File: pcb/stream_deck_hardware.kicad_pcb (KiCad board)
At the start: 2 copper layers, 16 parts, among them SW1 SW_Push_LED, SW10 SW_Push_LED, SW11 SW_Push_LED, SW3 SW_Push_LED, SW5 SW_Push_LED, SW6 SW_Push_LED, SW8 SW_Push_LED, SW9 SW_Push_LED

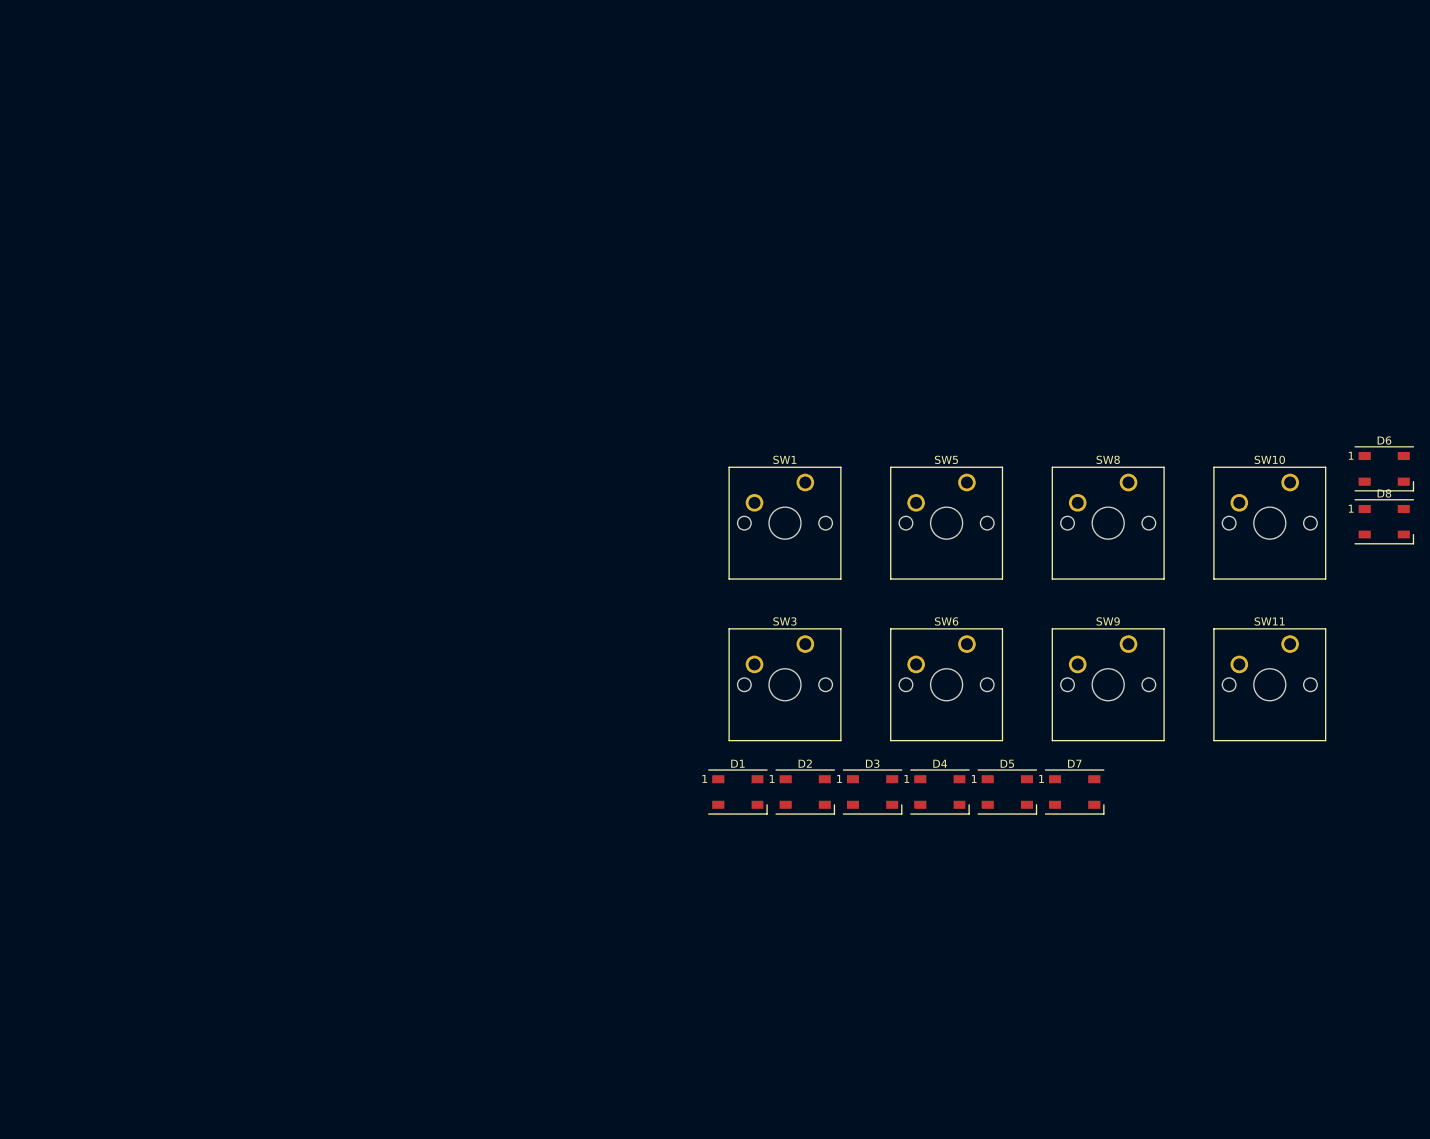
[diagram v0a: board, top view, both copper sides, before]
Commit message: Footprints update and some changes
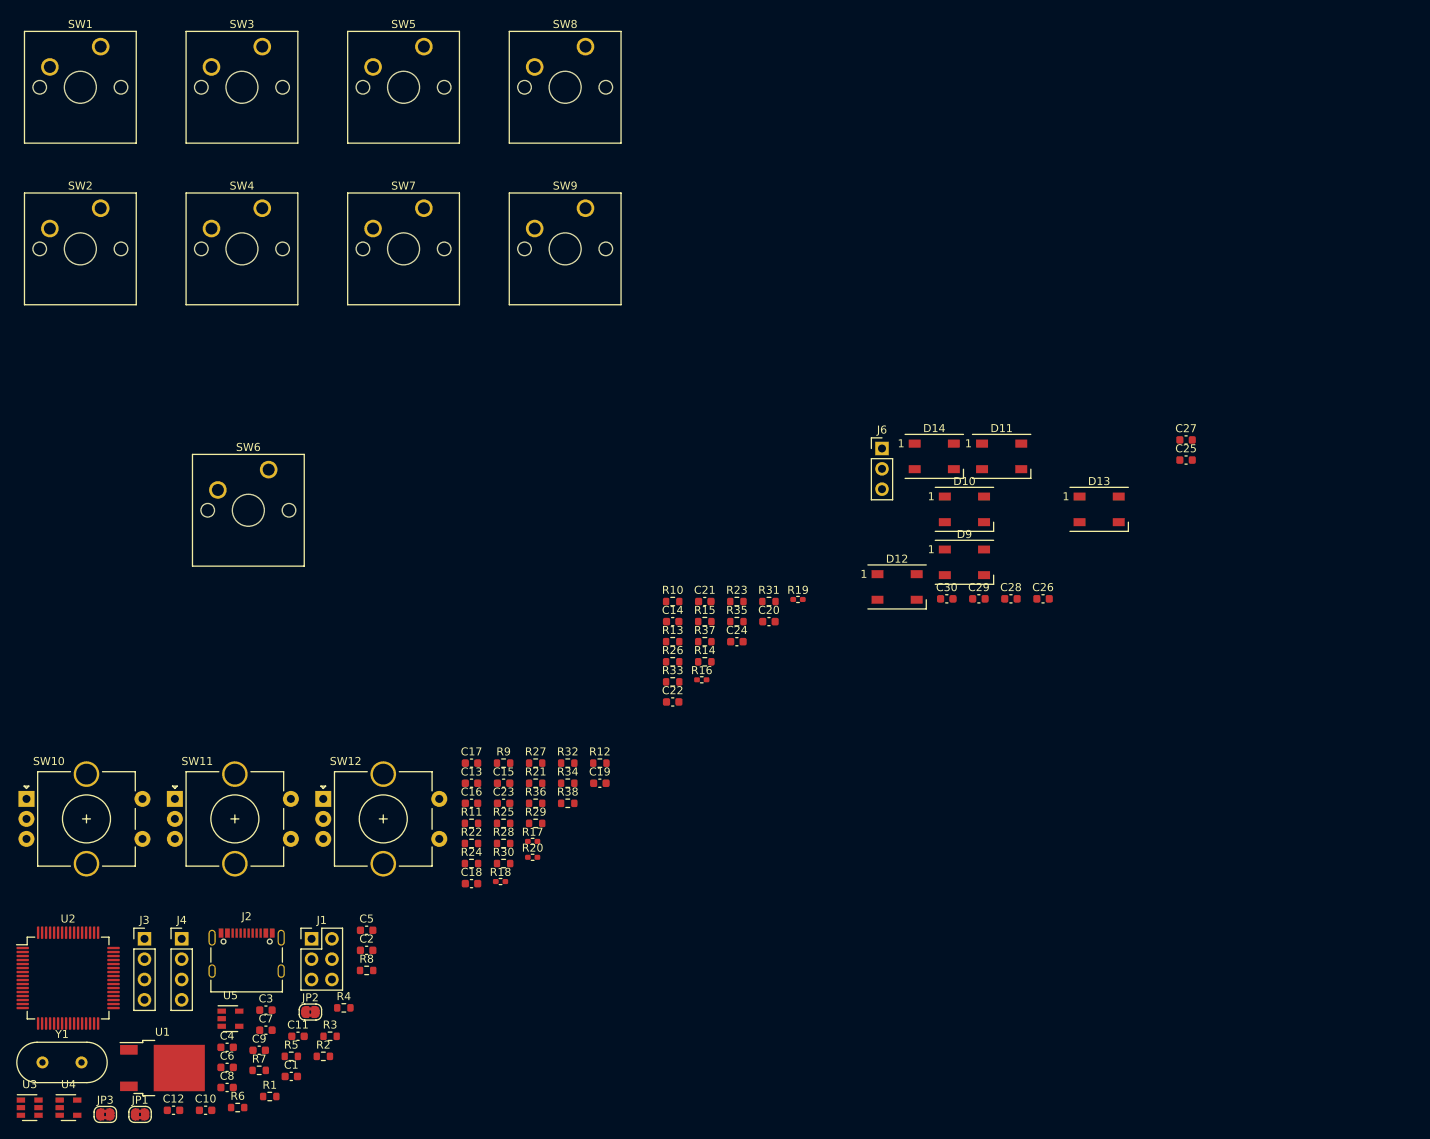
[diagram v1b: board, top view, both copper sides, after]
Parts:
- removed D1, D2, D3, D4, D5, D6, D7, D8: WS2812B, LED_SMD:LED_WS2812B_PLCC4_5.0x5.0mm_P3.2mm
- added C1: 100nF, Capacitor_SMD:C_0603_1608Metric, F.Cu at (56.2, 97.5)
- added C10: 25pF, Capacitor_SMD:C_0603_1608Metric, F.Cu at (45.5, 101.8)
- added C11: 25pF, Capacitor_SMD:C_0603_1608Metric, F.Cu at (57.0, 92.5)
- added C12: 0.1uF, Capacitor_SMD:C_0603_1608Metric, F.Cu at (41.5, 101.8)
- added C13: C, Capacitor_SMD:C_0603_1608Metric, F.Cu at (78.7, 60.9)
- added C14: C, Capacitor_SMD:C_0603_1608Metric, F.Cu at (103.9, 40.7)
- added C15: C, Capacitor_SMD:C_0603_1608Metric, F.Cu at (82.7, 60.9)
- added C16: C, Capacitor_SMD:C_0603_1608Metric, F.Cu at (78.7, 63.4)
- added C17: C, Capacitor_SMD:C_0603_1608Metric, F.Cu at (78.7, 58.4)
- added C18: C, Capacitor_SMD:C_0603_1608Metric, F.Cu at (78.7, 73.5)
- added C19: C, Capacitor_SMD:C_0603_1608Metric, F.Cu at (94.7, 60.9)
- added C2: 100nF, Capacitor_SMD:C_0603_1608Metric, F.Cu at (65.6, 81.8)
- added C20: C, Capacitor_SMD:C_0603_1608Metric, F.Cu at (115.9, 40.7)
- added C21: C, Capacitor_SMD:C_0603_1608Metric, F.Cu at (107.9, 38.2)
- added C22: C, Capacitor_SMD:C_0603_1608Metric, F.Cu at (103.9, 50.7)
- added C23: C, Capacitor_SMD:C_0603_1608Metric, F.Cu at (82.7, 63.4)
- added C24: C, Capacitor_SMD:C_0603_1608Metric, F.Cu at (111.9, 43.2)
- added C25: C, Capacitor_SMD:C_0603_1608Metric, F.Cu at (168.0, 20.5)
- added C26: C, Capacitor_SMD:C_0603_1608Metric, F.Cu at (150.1, 37.9)
- added C27: C, Capacitor_SMD:C_0603_1608Metric, F.Cu at (168.0, 18.0)
- added C28: C, Capacitor_SMD:C_0603_1608Metric, F.Cu at (146.1, 37.9)
- added C29: C, Capacitor_SMD:C_0603_1608Metric, F.Cu at (142.1, 37.9)
- added C3: 100nF, Capacitor_SMD:C_0603_1608Metric, F.Cu at (53.0, 89.3)
- added C30: C, Capacitor_SMD:C_0603_1608Metric, F.Cu at (138.1, 37.9)
- added C4: 100nF, Capacitor_SMD:C_0603_1608Metric, F.Cu at (48.2, 93.9)
- added C5: 100nF, Capacitor_SMD:C_0603_1608Metric, F.Cu at (65.6, 79.3)
- added C6: 100nF, Capacitor_SMD:C_0603_1608Metric, F.Cu at (48.2, 96.4)
- added C7: 0,1uF, Capacitor_SMD:C_0603_1608Metric, F.Cu at (53.0, 91.8)
- added C8: 2,2uF, Capacitor_SMD:C_0603_1608Metric, F.Cu at (48.2, 98.9)
- added C9: 4.7uF, Capacitor_SMD:C_0603_1608Metric, F.Cu at (52.2, 94.3)
- added D10: WS2812B, LED_SMD:LED_WS2812B_PLCC4_5.0x5.0mm_P3.2mm, F.Cu at (140.3, 26.7)
- added D11: WS2812B, LED_SMD:LED_WS2812B_PLCC4_5.0x5.0mm_P3.2mm, F.Cu at (145.0, 20.0)
- added D12: WS2812B, LED_SMD:LED_WS2812B_PLCC4_5.0x5.0mm_P3.2mm, F.Cu at (131.9, 36.4)
- added D13: WS2812B, LED_SMD:LED_WS2812B_PLCC4_5.0x5.0mm_P3.2mm, F.Cu at (157.2, 26.7)
- added D14: WS2812B, LED_SMD:LED_WS2812B_PLCC4_5.0x5.0mm_P3.2mm, F.Cu at (136.6, 20.0)
- added D9: WS2812B, LED_SMD:LED_WS2812B_PLCC4_5.0x5.0mm_P3.2mm, F.Cu at (140.3, 33.3)
- added J1: Conn_BOOT, Connector_PinHeader_2.54mm:PinHeader_2x03_P2.54mm_Vertical, F.Cu at (58.7, 80.3)
- added J2: USB_C_Receptacle_USB2.0, Connector_USB:USB_C_Receptacle_Palconn_UTC16-G, F.Cu at (50.6, 82.1)
- added J3: Conn_01x04_Male, Connector_PinHeader_2.54mm:PinHeader_1x04_P2.54mm_Vertical, F.Cu at (37.8, 80.3)
- added J4: Conn_01x04_Male, Connector_PinHeader_2.54mm:PinHeader_1x04_P2.54mm_Vertical, F.Cu at (42.5, 80.3)
- added J6: Conn_01x03_Female, Connector_PinHeader_2.54mm:PinHeader_1x03_P2.54mm_Vertical, F.Cu at (130.0, 19.1)
- added JP1: SolderJumper_2_Bridged, Jumper:SolderJumper-2_P1.3mm_Bridged2Bar_RoundedPad1.0x1.5mm, F.Cu at (37.3, 102.3)
- added JP2: SolderJumper_2_Bridged, Jumper:SolderJumper-2_P1.3mm_Bridged2Bar_RoundedPad1.0x1.5mm, F.Cu at (58.6, 89.5)
- added JP3: SolderJumper_2_Bridged, Jumper:SolderJumper-2_P1.3mm_Bridged2Bar_RoundedPad1.0x1.5mm, F.Cu at (32.9, 102.3)
- added R1: R, Resistor_SMD:R_0603_1608Metric, F.Cu at (53.5, 100.1)
- added R10: R, Resistor_SMD:R_0603_1608Metric, F.Cu at (103.9, 38.2)
- added R11: R, Resistor_SMD:R_0603_1608Metric, F.Cu at (78.7, 65.9)
- added R12: R, Resistor_SMD:R_0603_1608Metric, F.Cu at (94.7, 58.4)
- added R13: R, Resistor_SMD:R_0603_1608Metric, F.Cu at (103.9, 43.2)
- added R14: R, Resistor_SMD:R_0603_1608Metric, F.Cu at (107.9, 45.7)
- added R15: R, Resistor_SMD:R_0603_1608Metric, F.Cu at (107.9, 40.7)
- added R16: R, Resistor_SMD:R_0402_1005Metric_Pad0.72x0.64mm_HandSolder, F.Cu at (107.5, 48.0)
- added R17: R, Resistor_SMD:R_0402_1005Metric_Pad0.72x0.64mm_HandSolder, F.Cu at (86.3, 68.2)
- added R18: R, Resistor_SMD:R_0402_1005Metric_Pad0.72x0.64mm_HandSolder, F.Cu at (82.3, 73.2)
- added R19: R, Resistor_SMD:R_0402_1005Metric_Pad0.72x0.64mm_HandSolder, F.Cu at (119.5, 37.9)
- added R2: R, Resistor_SMD:R_0603_1608Metric, F.Cu at (60.2, 95.0)
- added R20: R, Resistor_SMD:R_0402_1005Metric_Pad0.72x0.64mm_HandSolder, F.Cu at (86.3, 70.2)
- added R21: R, Resistor_SMD:R_0603_1608Metric, F.Cu at (86.7, 60.9)
- added R22: R, Resistor_SMD:R_0603_1608Metric, F.Cu at (78.7, 68.4)
- added R23: R, Resistor_SMD:R_0603_1608Metric, F.Cu at (111.9, 38.2)
- added R24: R, Resistor_SMD:R_0603_1608Metric, F.Cu at (78.7, 70.9)
- added R25: R, Resistor_SMD:R_0603_1608Metric, F.Cu at (82.7, 65.9)
- added R26: R, Resistor_SMD:R_0603_1608Metric, F.Cu at (103.9, 45.7)
- added R27: R, Resistor_SMD:R_0603_1608Metric, F.Cu at (86.7, 58.4)
- added R28: R, Resistor_SMD:R_0603_1608Metric, F.Cu at (82.7, 68.4)
- added R29: R, Resistor_SMD:R_0603_1608Metric, F.Cu at (86.7, 65.9)
- added R3: 5.1k, Resistor_SMD:R_0603_1608Metric, F.Cu at (61.0, 92.5)
- added R30: R, Resistor_SMD:R_0603_1608Metric, F.Cu at (82.7, 70.9)
- added R31: R, Resistor_SMD:R_0603_1608Metric, F.Cu at (115.9, 38.2)
- added R32: R, Resistor_SMD:R_0603_1608Metric, F.Cu at (90.7, 58.4)
- added R33: R, Resistor_SMD:R_0603_1608Metric, F.Cu at (103.9, 48.2)
- added R34: R, Resistor_SMD:R_0603_1608Metric, F.Cu at (90.7, 60.9)
- added R35: R, Resistor_SMD:R_0603_1608Metric, F.Cu at (111.9, 40.7)
- added R36: R, Resistor_SMD:R_0603_1608Metric, F.Cu at (86.7, 63.4)
- added R37: R, Resistor_SMD:R_0603_1608Metric, F.Cu at (107.9, 43.2)
- added R38: R, Resistor_SMD:R_0603_1608Metric, F.Cu at (90.7, 63.4)
- added R4: 5.1k, Resistor_SMD:R_0603_1608Metric, F.Cu at (62.7, 89.0)
- added R5: R, Resistor_SMD:R_0603_1608Metric, F.Cu at (56.2, 95.0)
- added R6: 4k7, Resistor_SMD:R_0603_1608Metric, F.Cu at (49.5, 101.4)
- added R7: 4k7, Resistor_SMD:R_0603_1608Metric, F.Cu at (52.2, 96.8)
- added R8: 4k7, Resistor_SMD:R_0603_1608Metric, F.Cu at (65.6, 84.3)
- added R9: R, Resistor_SMD:R_0603_1608Metric, F.Cu at (82.7, 58.4)
- added SW12: EN_03, Rotary_Encoder:RotaryEncoder_Alps_EC11E-Switch_Vertical_H20mm_CircularMountingHoles, F.Cu at (60.2, 62.9)
- added SW2: SW_Push, Button_Switch_Keyboard:SW_Cherry_MX_1.00u_PCB, F.Cu at (32.4, -11.0)
- added SW4: SW_Push, Button_Switch_Keyboard:SW_Cherry_MX_1.00u_PCB, F.Cu at (52.5, -11.0)
- added SW7: SW_Push, Button_Switch_Keyboard:SW_Cherry_MX_1.00u_PCB, F.Cu at (72.8, -11.0)
- added U1: LF33_TO252, Package_TO_SOT_SMD:TO-252-2, F.Cu at (40.1, 96.5)
- added U2: STM32F401RCTx, Package_QFP:LQFP-64_10x10mm_P0.5mm, F.Cu at (28.3, 85.2)
- added U3: 74LVC1G332, Package_TO_SOT_SMD:SOT-23-6, F.Cu at (23.5, 101.5)
- added U4: AT24CS02-STUM, Package_TO_SOT_SMD:SOT-23-5, F.Cu at (28.3, 101.5)
- added U5: AT24CS02-STUM, Package_TO_SOT_SMD:SOT-23-5, F.Cu at (48.6, 90.3)
- added Y1: Crystal_Small, Crystal:Crystal_HC49-U_Vertical, F.Cu at (25.1, 95.8)
- SW1, SW3, SW5, SW6, SW8, SW9: value SW_Push_LED -> SW_Push
- SW10: value SW_Push_LED -> EN_01; footprint Button_Switch_Keyboard:SW_Cherry_MX_1.00u_PCB -> Rotary_Encoder:RotaryEncoder_Alps_EC11E-Switch_Vertical_H20mm_CircularMountingHoles
- SW11: value SW_Push_LED -> EN_02; footprint Button_Switch_Keyboard:SW_Cherry_MX_1.00u_PCB -> Rotary_Encoder:RotaryEncoder_Alps_EC11E-Switch_Vertical_H20mm_CircularMountingHoles
- moved SW10 162.8 mm to (23.1, 62.9)
- moved SW11 140.7 mm to (41.6, 62.9)
- moved SW1 103.6 mm to (32.4, -31.2)
- moved SW3 100.9 mm to (52.5, -31.2)
- moved SW6 90.0 mm to (53.4, 21.7)
- moved SW8 87.0 mm to (93.0, -31.2)
- moved SW9 87.0 mm to (93.0, -11.0)
- moved SW5 87.0 mm to (72.8, -31.2)
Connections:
- SW1 pad 1: (no net) -> Net-(C13-Pad1)
- SW1 pad 2: (no net) -> GND
- SW3 pad 1: (no net) -> Net-(C15-Pad1)
- SW3 pad 2: (no net) -> GND
- SW5 pad 1: (no net) -> Net-(C17-Pad1)
- SW5 pad 2: (no net) -> GND
- SW6 pad 1: (no net) -> Net-(C18-Pad1)
- SW6 pad 2: (no net) -> GND
- SW8 pad 1: (no net) -> Net-(C20-Pad1)
- SW8 pad 2: (no net) -> GND
- SW9 pad 1: (no net) -> Net-(C21-Pad1)
- SW9 pad 2: (no net) -> GND

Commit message: PCB edges prototype
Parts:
- moved R3 200.0 mm to (254.5, 143.3)
- moved R4 198.4 mm to (254.7, 138.9)
- moved C5 196.2 mm to (254.8, 131.2)
- moved C2 196.2 mm to (254.8, 133.7)
- moved R8 196.2 mm to (254.8, 136.2)
- moved C14 165.4 mm to (254.0, 110.1)
- moved C20 165.4 mm to (266.1, 110.1)
- moved C21 165.4 mm to (258.0, 107.6)
- moved C22 165.4 mm to (254.0, 120.1)
- moved C24 165.4 mm to (262.1, 112.6)
- moved R10 165.4 mm to (254.0, 107.6)
- moved R13 165.4 mm to (254.0, 112.6)
- moved R14 165.4 mm to (258.0, 115.1)
- moved R15 165.4 mm to (258.0, 110.1)
- moved R16 165.4 mm to (257.7, 117.3)
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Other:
- board outline added: 70 x 100 mm

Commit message: Components positioning
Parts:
- removed SW10: EN_01, Rotary_Encoder:RotaryEncoder_Alps_EC11E-Switch_Vertical_H20mm_CircularMountingHoles
- added J5: Conn_01x05_Male, Connector_PinHeader_2.54mm:PinHeader_1x05_P2.54mm_Horizontal, F.Cu at (56.6, 70.0)
- added REF**: MountingHole_2.2mm_M2_DIN965_Pad, MountingHole:MountingHole_2.2mm_M2_DIN965_Pad, F.Cu at (71.9, 71.8)
- added REF**: MountingHole_2.2mm_M2_DIN965_Pad, MountingHole:MountingHole_2.2mm_M2_DIN965_Pad, F.Cu at (122.4, 142.8)
- added REF**: MountingHole_2.2mm_M2_DIN965_Pad, MountingHole:MountingHole_2.2mm_M2_DIN965_Pad, F.Cu at (56.8, 142.8)
- added REF**: MountingHole_2.2mm_M2_DIN965_Pad, MountingHole:MountingHole_2.2mm_M2_DIN965_Pad, F.Cu at (122.4, 47.3)
- moved D11 184.2 mm to (77.5, 131.0), turned to 90 degrees
- moved D9 168.4 mm to (77.5, 108.0), turned to 90 degrees
- moved D10 165.5 mm to (77.5, 85.0), turned to 90 degrees
- moved D13 163.1 mm to (101.5, 108.0), turned to 90 degrees
- moved J6 160.4 mm to (71.0, 51.2)
- moved D12 143.7 mm to (101.5, 131.0), turned to 90 degrees
- moved D14 139.2 mm to (101.5, 85.0), turned to 90 degrees
- moved ENC2 138.4 mm to (74.4, 51.3)
- moved J2 134.0 mm to (95.8, 48.5), turned to 180 degrees
- moved ENC3 129.7 mm to (102.7, 51.2)
- moved JP3 129.1 mm to (83.2, 70.3)
- moved U3 124.4 mm to (79.0, 70.6)
- moved Y1 123.8 mm to (81.3, 65.0), turned to 180 degrees
- moved U5 116.3 mm to (111.3, 63.6)
- moved U4 113.8 mm to (107.1, 63.6)
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- renumbered SW11 to ENC2, SW12 to ENC3
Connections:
- D14 pad 2: (no net) -> Net-(D14-Pad2)
- J2 pad A8: (no net) -> Net-(J2-PadA8)
- J2 pad B8: (no net) -> Net-(J2-PadB8)
- U2 pad 16: (no net) -> Net-(U2-Pad16)
- U2 pad 17: (no net) -> Net-(U2-Pad17)
- U2 pad 2: (no net) -> Net-(U2-Pad2)
- U2 pad 20: (no net) -> Net-(U2-Pad20)
- U2 pad 21: (no net) -> Net-(U2-Pad21)
- U2 pad 26: (no net) -> Net-(U2-Pad26)
- U2 pad 27: (no net) -> Net-(U2-Pad27)
- U2 pad 29: (no net) -> Net-(U2-Pad29)
- U2 pad 3: (no net) -> Net-(U2-Pad3)
- U2 pad 33: (no net) -> Net-(U2-Pad33)
- U2 pad 34: (no net) -> Net-(U2-Pad34)
- U2 pad 35: (no net) -> Net-(U2-Pad35)
- U2 pad 36: (no net) -> Net-(U2-Pad36)
- U2 pad 4: (no net) -> Net-(U2-Pad4)
- U2 pad 40: (no net) -> Net-(U2-Pad40)
- U2 pad 43: (no net) -> Net-(U2-Pad43)
- U2 pad 50: (no net) -> Net-(U2-Pad50)
- U2 pad 54: (no net) -> Net-(U2-Pad54)
- U2 pad 55: (no net) -> Net-(U2-Pad55)
- U2 pad 56: (no net) -> Net-(U2-Pad56)
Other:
- outline, holes or cut-outs redrawn

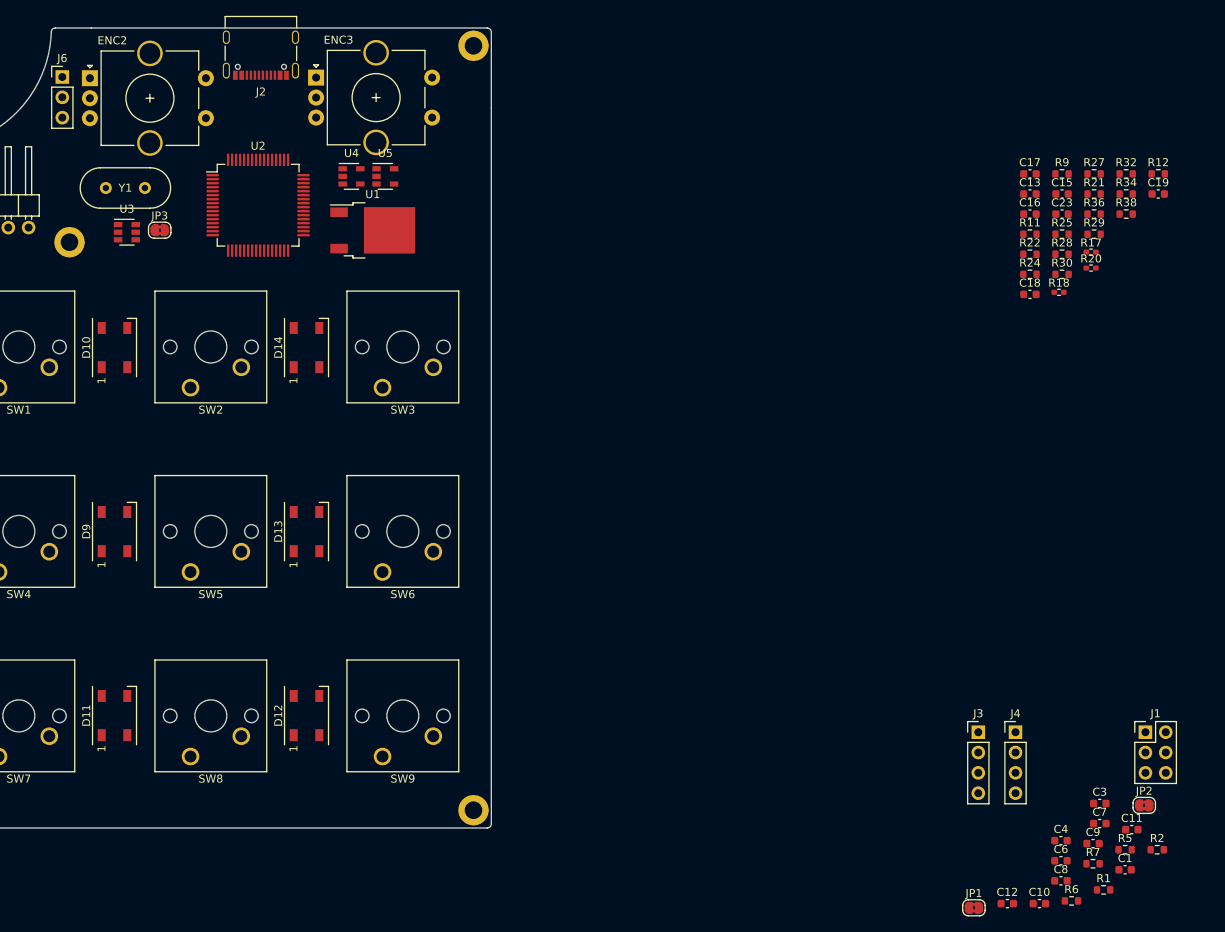
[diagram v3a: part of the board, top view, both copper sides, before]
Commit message: Components placement
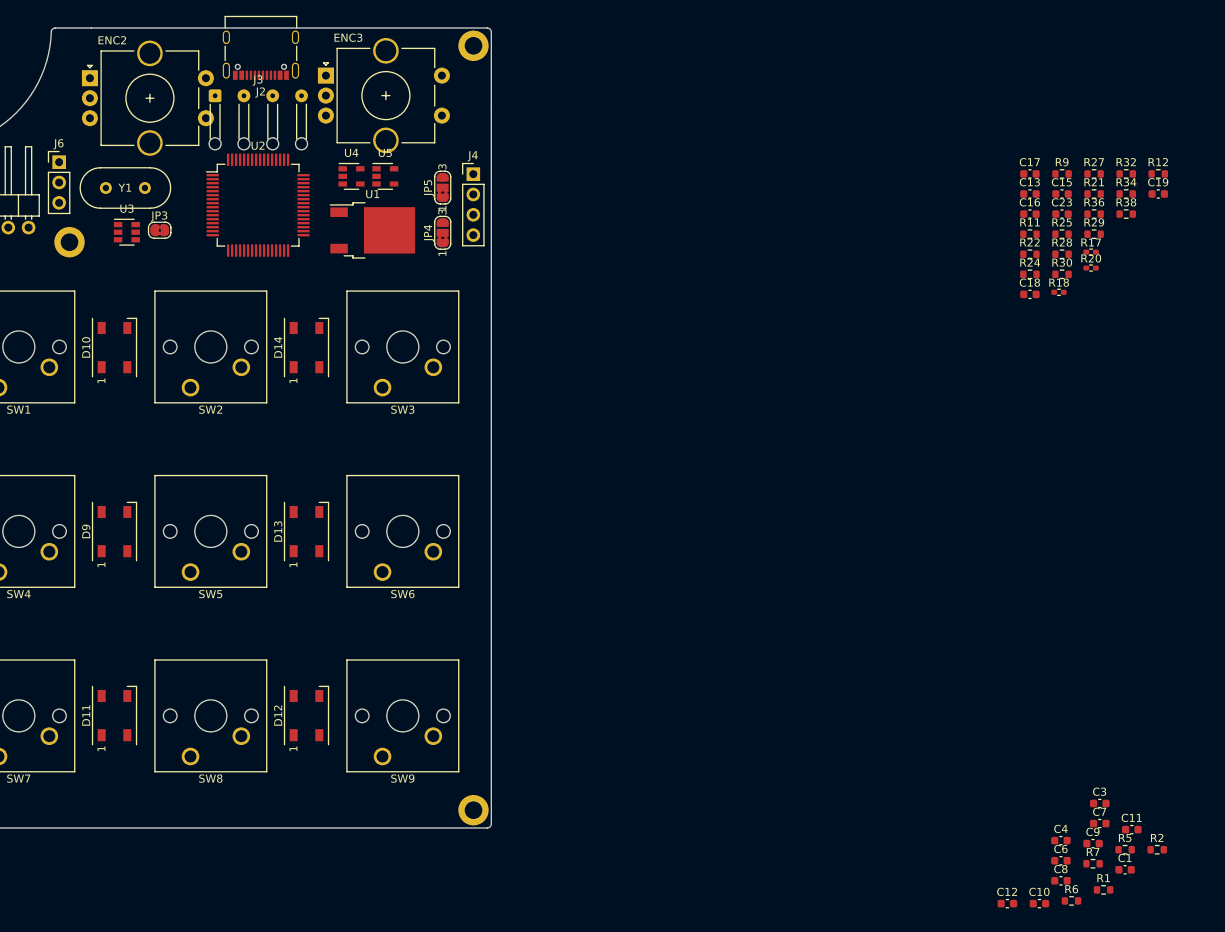
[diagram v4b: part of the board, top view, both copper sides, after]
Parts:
- removed J1: Conn_BOOT, Connector_PinHeader_2.54mm:PinHeader_2x03_P2.54mm_Vertical
- removed JP1, JP2: SolderJumper_2_Bridged, Jumper:SolderJumper-2_P1.3mm_Bridged2Bar_RoundedPad1.0x1.5mm
- added JP4: SolderJumper_3_Open, Jumper:SolderJumper-3_P1.3mm_Bridged2Bar12_RoundedPad1.0x1.5mm_NumberLabels, F.Cu at (118.5, 70.7)
- added JP5: SolderJumper_3_Open, Jumper:SolderJumper-3_P1.3mm_Bridged2Bar12_RoundedPad1.0x1.5mm_NumberLabels, F.Cu at (118.5, 65.0)
- J3: footprint Connector_PinHeader_2.54mm:PinHeader_1x04_P2.54mm_Vertical -> Connector_Wire:SolderWire-0.1sqmm_1x04_P3.6mm_D0.4mm_OD1mm_Relief
- moved J3 124.2 mm to (90.1, 53.5)
- moved J4 97.3 mm to (122.3, 63.3)
- moved J6 10.7 mm to (70.6, 61.8)
- moved ENC3 1.25 mm to (103.9, 51.0)
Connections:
- J2 pad A6: Net-(J2-PadA6) -> USB_DP
- J2 pad A7: Net-(J2-PadA7) -> USB_DM
- J2 pad B6: Net-(J2-PadA6) -> USB_DP
- J2 pad B7: Net-(J2-PadA7) -> USB_DM
